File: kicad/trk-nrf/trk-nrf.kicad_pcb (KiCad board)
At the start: 2 copper layers, 35 x 25 mm, 42 parts, among them U1 nRF9151-LAXX, U2 CDCE6214RGER, U3 TPS631010YBGR, U4 TPS631010YBGR, X1 TG2520SMN-xx.xxxxxxMhz-xxxxNM

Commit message: Updates - pre-routing
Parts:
- added J1: Conn_02x05_Odd_Even, Connector_PinHeader_1.00mm:PinHeader_2x05_P1.00mm_Vertical_SMD, B.Cu at (166.6, 91.7)
- C1: footprint Capacitor_SMD:C_1206_3216Metric -> Capacitor_SMD:C_0805_2012Metric
- R11: footprint Resistor_SMD:R_0603_1608Metric -> Resistor_SMD:R_0402_1005Metric
- TP1, TP2: footprint TestPoint:TestPoint_THTPad_D2.5mm_Drill1.2mm -> TestPoint:TestPoint_Pad_1.5x1.5mm
- TP3: value WSPR N -> WSPR_ANT_N
- TP4: value WSPR P -> WSPR _ANT_P
- TP5, TP6: footprint TestPoint:TestPoint_THTPad_D2.5mm_Drill1.2mm -> TestPoint:TestPoint_THTPad_D1.5mm_Drill0.7mm
- U3, U4: footprint footprints:YBG0008-MFG -> footprints:YBG0008
- moved R7 135.4 mm to (172.0, 105.5), turned to 90 degrees
- moved C7 134.2 mm to (170.5, 106.0), turned to 180 degrees
- moved C12 133.8 mm to (170.5, 105.0), turned to 180 degrees
- moved R8 132.2 mm to (172.0, 97.5), turned to -90 degrees
- moved C8 131.5 mm to (172.0, 95.5), turned to 90 degrees
- moved TP3 128.9 mm to (170.5, 108.0)
- moved R9 127.2 mm to (167.0, 96.5), turned to 90 degrees
- moved TP1 125.6 mm to (166.5, 108.6)
- moved R1 124.6 mm to (165.2, 93.8), turned to 90 degrees
- moved R2 123.9 mm to (165.2, 91.8), turned to 90 degrees
- moved R11 123.4 mm to (170.0, 94.0), turned to 90 degrees
- moved TP4 123.0 mm to (170.6, 90.8), turned to 180 degrees
- moved C11 122.5 mm to (162.8, 94.5)
- moved R10 122.0 mm to (155.5, 108.5)
- moved TP2 121.9 mm to (162.4, 108.6)
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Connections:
- net /TCXO_REFCLK renamed Net-(U2A-PRIREF_P)
- net Net-(U1-ENABLE) renamed /+3.3V_Ferrite
- net Net-(U1-~{RESET}) renamed /nRF_nRESET
- net Net-(U3-FB) renamed /FB_1.8
- net Net-(U4-FB) renamed /FB_3.3
- R14 pad 2: unconnected-(R14-Pad2) -> /MON_V3P3
- U1 pad 53: unconnected-(U1-COEX1-Pad53) -> /1PPS
- U1 pad 64: unconnected-(U1-P0.07-Pad64) -> /1PPS
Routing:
- net GND: vias 0 -> 10
- added copper zone on F.Cu, net GND
- added copper zone on In2.Cu, net VBUS
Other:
- board size 35 x 25 mm -> 23.2 x 22 mm
- copper layers 2 -> 4

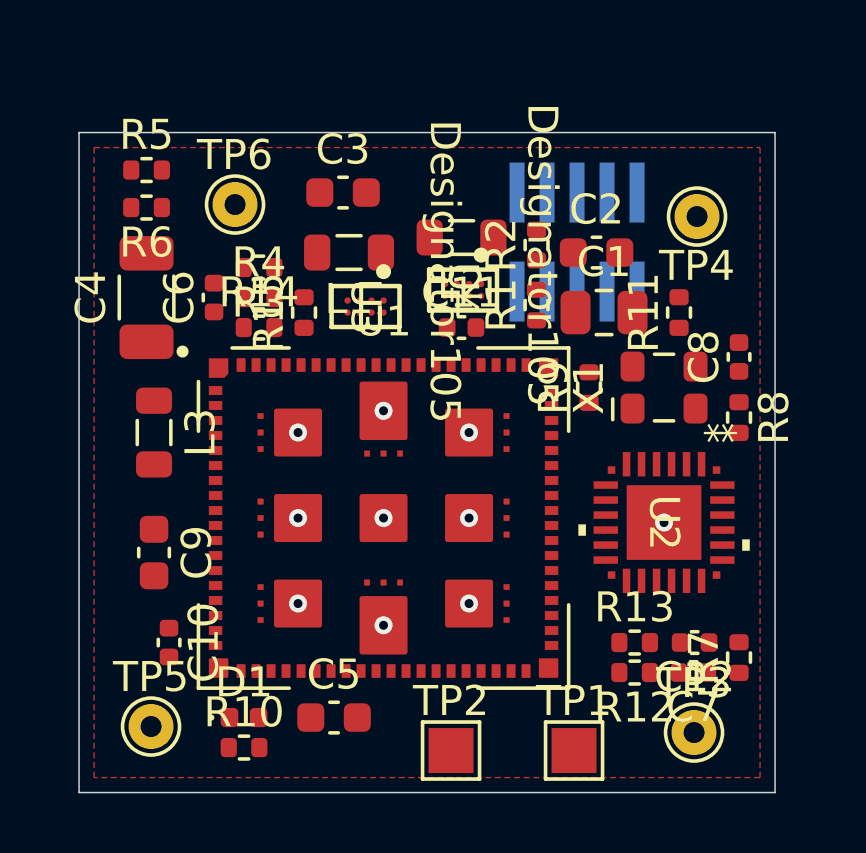
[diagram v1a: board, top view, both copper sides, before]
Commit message: Schematic edits and drc changes
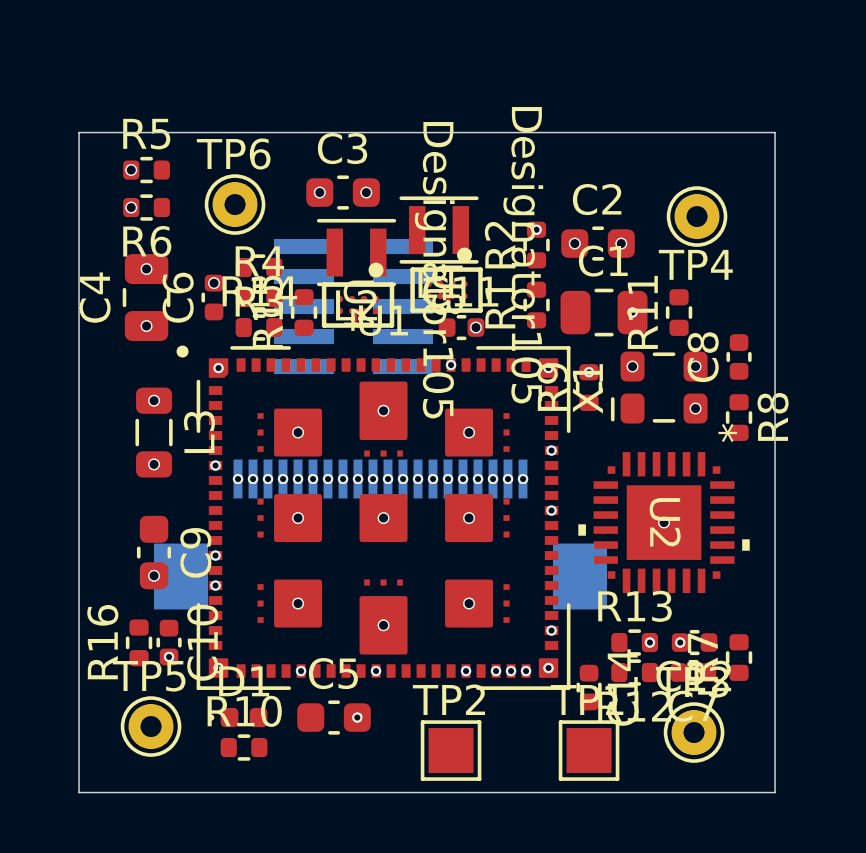
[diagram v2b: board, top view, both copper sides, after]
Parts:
- added C14: 39pF, Capacitor_SMD:C_0402_1005Metric, F.Cu at (167.0, 106.5)
- added J2: Conn_01x20_Pin, Connector_FFC-FPC:Hirose_FH12-20S-0.5SH_1x20-1MP_P0.50mm_Horizontal, B.Cu at (160.1, 101.4)
- added R16: 91K, Resistor_SMD:R_0402_1005Metric, F.Cu at (152.0, 105.0)
- C4: footprint Capacitor_SMD:C_1206_3216Metric -> Capacitor_SMD:C_0805_2012Metric
- C7, C8: value 100nF -> .1uF
- L1, L2: value 2.0uH -> 1.0uH; footprint Inductor_SMD:L_0805_2012Metric -> Inductor_SMD:L_Murata_DFE201610P
- moved J1 7.75 mm to (159.2, 93.8), turned to 0 degrees
- moved L2 3.54 mm to (159.2, 92.0)
- moved U4 3.54 mm to (159.3, 93.8)
- moved L1 3.09 mm to (162.0, 91.2)
- moved U3 2.76 mm to (162.2, 93.2)
- moved TP1 0.50 mm to (167.0, 108.6)
- moved C2 0.30 mm to (167.3, 91.7)
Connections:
- net Net-(U2A-PRIREF_P) renamed /TCXO_REFCLK
- C1 pad 1: +1V8 -> +1.8V
- C11 pad 1: +1V8 -> +1.8V
- J1 pad 7: /nrf_nRESET -> /nRF_nRESET
- J1 pad 9: /+1.8V -> +1.8V
- R1 pad 1: +1V8 -> +1.8V
- R10 pad 1: +1V8 -> +1.8V
- R11 pad 1: +1V8 -> +1.8V
- R12 pad 1: +1V8 -> +1.8V
- TP1 pad 1: Net-(U1-GPS) -> Net-(C14-Pad2)
- U1 pad 10: /+3.3V_Ferrite -> Net-(U1-ENABLE)
- U1 pad 19: +1V8 -> +1.8V
- U1 pad 2: unconnected-(U1-P0.20/AIN7-Pad2) -> /AIN7
- U1 pad 44: unconnected-(U1-P0.26-Pad44) -> /P0.26
- U1 pad 45: unconnected-(U1-P0.27-Pad45) -> /P0.27
- U1 pad 47: unconnected-(U1-P0.28-Pad47) -> /P0.28
- U1 pad 48: unconnected-(U1-P0.29-Pad48) -> /P0.29
- U1 pad 49: unconnected-(U1-P0.30-Pad49) -> /P0.30
- U1 pad 65: +1V8 -> +1.8V
- U1 pad 67: unconnected-(U1-P0.08-Pad67) -> /PO.08
- U1 pad 68: unconnected-(U1-P0.09-Pad68) -> /P0.09
- U1 pad 69: unconnected-(U1-P0.10-Pad69) -> /P0.10
- U1 pad 70: unconnected-(U1-P0.11-Pad70) -> /P0.11
- U1 pad 72: unconnected-(U1-P0.12-Pad72) -> /P0.12
- U1 pad 77: unconnected-(U1-P0.16/AIN3-Pad77) -> /AIN3
- U1 pad 78: unconnected-(U1-P0.17/AIN4-Pad78) -> /AIN4
- U1 pad 79: unconnected-(U1-P0.18/AIN5-Pad79) -> /AIN5
- U1 pad 80: unconnected-(U1-P0.19/AIN6-Pad80) -> /AIN6
- U2 pad 12: /SCLK -> /SCL
- U3 pad D1: +1V8 -> +1.8V
- X1 pad 4: +1V8 -> +1.8V
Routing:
- net GND: track 0.00 -> 1.50 mm, vias 10 -> 44
- net VBUS: vias 0 -> 4
- net /TCXO_REFCLK: vias 0 -> 1
- net /PO.08: vias 0 -> 1
- net /P0.30: vias 0 -> 1
- net /P0.29: vias 0 -> 1
- net /P0.28: vias 0 -> 1
- net /P0.27: vias 0 -> 1
- net /P0.26: vias 0 -> 1
- net /P0.12: vias 0 -> 1
- net /P0.11: vias 0 -> 1
- net /P0.10: vias 0 -> 1
- net /P0.09: vias 0 -> 1
- net /AIN7: vias 0 -> 1
- net /AIN6: vias 0 -> 1
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- added copper zone on In1.Cu, net GND
- removed copper zone on F.Cu, net GND
- removed copper zone on In2.Cu, net VBUS

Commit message: Updated schematic
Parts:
- moved J1 0.81 mm to (159.1, 93.0)
- moved TP6 0.71 mm to (154.5, 90.3)
- turned X1 to -90 degrees
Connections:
- J2 pad 12: /AIN7 -> /MON_VBUS
- U1 pad 2: /AIN7 -> /MON_VBUS
- U1 pad 73: /MON_VBUS -> /AIN0
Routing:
- net GND: vias 44 -> 45
- net /TCXO_REFCLK: vias 1 -> 0
- net /PO.08: vias 1 -> 2
- net /PLL_GPIO4: vias 0 -> 1
- net /P0.11: vias 1 -> 2
- net /P0.10: vias 1 -> 2
- net /P0.09: vias 1 -> 2
- net /MON_VBUS: vias 0 -> 1
- net /MON_V1P8: vias 0 -> 1
- net /AIN7: vias 1 -> 0
- net /AIN6: vias 1 -> 2
- net /AIN5: vias 1 -> 2
- net /AIN4: vias 1 -> 2
- net /AIN3: vias 1 -> 2
- net /1PPS: vias 0 -> 1
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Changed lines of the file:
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@@
 	(net 57 "unconnected-(U1-VIO-Pad29)")
 	(net 58 "/AIN5")
-	(net 59 "/AIN7")
+	(net 59 "/AIN0")
 	(net 60 "unconnected-(U1-COEX2-Pad54)")
 	(net 61 "unconnected-(U2A-OUT2_P-Pad18)")
@@
 	(footprint "TestPoint:TestPoint_THTPad_D1.5mm_Drill0.7mm"
 		(layer "F.Cu")
-		(at 155.2 90.4)
+		(at 154.5 90.3)
 		(descr "THT pad as test Point, diameter 1.5mm, hole diameter 0.7mm")
 		(tags "test point THT pad")
@@
 			(layers "F.Cu" "F.Paste" "F.Mask")
 			(roundrect_rratio 0.05)
-			(net 59 "/AIN7")
+			(net 95 "/MON_VBUS")
 			(pinfunction "P0.20/AIN7")
 			(pintype "bidirectional")
@@
 			(layers "F.Cu" "F.Paste" "F.Mask")
 			(roundrect_rratio 0.05)
-			(net 95 "/MON_VBUS")
+			(net 59 "/AIN0")
 			(pinfunction "P0.13/AIN0")
 			(pintype "bidirectional")
@@
 		(placed yes)
 		(layer "F.Cu")
-		(at 169.5 96.5 90)
+		(at 169.5 96.5 -90)
 		(descr "Miniature Crystal Clock Oscillator TG2520 series, https://support.epson.biz/td/api/doc_check.php?dl=app_TG2520SMN&lang=en")
 		(tags "Miniature Crystal Clock Oscillator TG2520 series SMD SMT")
@@
 		)
 		(property "Footprint" "Oscillator:Oscillator_SMD_SeikoEpson_TG2520SMN-xxx-xxxxxx-4Pin_2.5x2.0mm"
-			(at 0 0 90)
+			(at 0 0 -90)
 			(unlocked yes)
 			(layer "F.Fab")
@@
 		)
 		(property "Datasheet" "https://support.epson.biz/td/api/doc_check.php?dl=app_TG2520SMN&lang=en"
-			(at 0 0 90)
+			(at 0 0 -90)
 			(unlocked yes)
 			(layer "F.Fab")
@@
 		)
 		(property "Description" "Crystal Oscillator Low Profile / High Stability TCXO"
-			(at 0 0 90)
+			(at 0 0 -90)
 			(unlocked yes)
 			(layer "F.Fab")
@@
 		)
 		(property "JLCPCB Part Number" "C3007519"
-			(at 0 0 90)
+			(at 0 0 -90)
 			(unlocked yes)
 			(layer "F.Fab")
@@
 		(attr smd)
 		(fp_line
-			(start -0.38 -1.71)
-			(end -1.07 -1.71)
+			(start -1.11 0.32)
+			(end -1.11 -0.32)
 			(stroke
 				(width 0.12)
@@
 		)
 		(fp_line
-			(start -1.11 0.32)
-			(end -1.11 -0.32)
+			(start -0.38 -1.71)
+			(end -1.07 -1.71)
 			(stroke
 				(width 0.12)
@@
 		)
 		(fp_line
-			(start 1.45 -1.7)
+			(start -1.45 1.7)
 			(end 1.45 1.7)
 			(stroke
@@
 		(fp_line
 			(start -1.45 -1.7)
-			(end 1.45 -1.7)
+			(end -1.45 1.7)
 			(stroke
 				(width 0.05)
@@
 		(fp_line
 			(start -1.45 -1.7)
-			(end -1.45 1.7)
+			(end 1.45 -1.7)
 			(stroke
 				(width 0.05)
@@
 		)
 		(fp_line
-			(start -1.45 1.7)
+			(start 1.45 -1.7)
 			(end 1.45 1.7)
 			(stroke
@@
 		)
 		(fp_line
-			(start 1 -1.25)
+			(start -1 1.25)
 			(end 1 1.25)
 			(stroke
@@
 		)
 		(fp_line
-			(start -0.5 -1.25)
-			(end 1 -1.25)
+			(start -1 -0.75)
+			(end -1 1.25)
 			(stroke
 				(width 0.1)
@@
 		)
 		(fp_line
-			(start -1 -0.75)
-			(end -1 1.25)
+			(start -0.5 -1.25)
+			(end 1 -1.25)
 			(stroke
 				(width 0.1)
@@
 		)
 		(fp_line
-			(start -1 1.25)
+			(start 1 -1.25)
 			(end 1 1.25)
 			(stroke
@@
 		)
 		(fp_text user "${REFERENCE}"
-			(at 0 0 0)
+			(at 0 0 360)
 			(layer "F.Fab")
 			(effects
@@
 		)
 		(pad "1" smd roundrect
-			(at -0.7 -1.05 90)
+			(at -0.7 -1.05 270)
 			(size 1 0.8)
 			(layers "F.Cu" "F.Paste" "F.Mask")
@@
 		)
 		(pad "2" smd roundrect
-			(at -0.7 1.05 90)
+			(at -0.7 1.05 270)
 			(size 1 0.8)
 			(layers "F.Cu" "F.Paste" "F.Mask")
@@
 		)
 		(pad "3" smd roundrect
-			(at 0.7 1.05 90)
+			(at 0.7 1.05 270)
 			(size 1 0.8)
 			(layers "F.Cu" "F.Paste" "F.Mask")
@@
 		)
 		(pad "4" smd roundrect
-			(at 0.7 -1.05 90)
+			(at 0.7 -1.05 270)
 			(size 1 0.8)
 			(layers "F.Cu" "F.Paste" "F.Mask")
@@
 			(polygon
 				(pts
-					(xy 168.2 96.65) (xy 168.2 96.35) (xy 168.9 96.35) (xy 168.9 95.5) (xy 170.1 95.5) (xy 170.1 96.35)
-					(xy 170.75 96.35) (xy 170.75 96.65) (xy 170.1 96.65) (xy 170.1 97.5) (xy 168.9 97.5) (xy 168.9 96.65)
+					(xy 170.8 96.35) (xy 170.8 96.65) (xy 170.1 96.65) (xy 170.1 97.5) (xy 168.9 97.5) (xy 168.9 96.65)
+					(xy 168.25 96.65) (xy 168.25 96.35) (xy 168.9 96.35) (xy 168.9 95.5) (xy 170.1 95.5) (xy 170.1 96.35)
 				)
 			)
@@
 	(footprint "Connector_PinHeader_1.00mm:PinHeader_2x05_P1.00mm_Vertical_SMD"
 		(layer "B.Cu")
-		(at 159.15 93.8)
+		(at 159.05 93)
 		(descr "surface-mounted straight pin header, 2x05, 1.00mm pitch, double rows")
 		(tags "Surface mounted pin header SMD 2x05 1.00mm double row")
@@
 			(size 0.3 1.3)
 			(layers "B.Cu" "B.Paste" "B.Mask")
-			(net 59 "/AIN7")
+			(net 95 "/MON_VBUS")
 			(pinfunction "Pin_12")
 			(pintype "passive")
@@
 	)
 	(via
+		(at 156.9 95.75)
+		(size 0.35)
+		(drill 0.2)
+		(layers "F.Cu" "B.Cu")
+		(net 21)
+	)
+	(via
 		(at 161.3 99.55)
 		(size 0.35)
@@
 	)
 	(via
+		(at 163.4 95.75)
+		(size 0.35)
+		(drill 0.2)
+		(layers "F.Cu" "B.Cu")
+		(net 23)
+	)
+	(via
 		(at 157.3 99.55)
 		(size 0.35)
@@
 	)
 	(via
+		(at 161.9 95.75)
+		(size 0.35)
+		(drill 0.2)
+		(layers "F.Cu" "B.Cu")
+		(net 25)
+	)
+	(via
 		(at 163.8 99.55)
 		(size 0.35)
@@
 	)
 	(via
+		(at 160.4 95.75)
+		(size 0.35)
+		(drill 0.2)
+		(layers "F.Cu" "B.Cu")
+		(net 37)
+	)
+	(via
 		(at 162.3 99.55)
 		(size 0.35)
@@
 	)
 	(via
+		(at 160.9 95.75)
+		(size 0.35)
+		(drill 0.2)
+		(layers "F.Cu" "B.Cu")
+		(net 47)
+	)
+	(via
 		(at 163.3 99.55)
 		(size 0.35)
@@
 	)
 	(via
+		(at 161.4 95.75)
+		(size 0.35)
+		(drill 0.2)
+		(layers "F.Cu" "B.Cu")
+		(net 49)
+	)
+	(via
+		(at 155.4 95.75)
+		(size 0.35)
+		(drill 0.2)
+		(layers "F.Cu" "B.Cu")
+		(net 52)
+	)
+	(via
 		(at 159.8 99.55)
 		(size 0.35)
@@
 	)
 	(via
-		(at 159.3 99.55)
+		(at 155.9 95.75)
 		(size 0.35)
 		(drill 0.2)
 		(layers "F.Cu" "B.Cu")
-		(net 59)
+		(net 58)
 	)
 	(segment
@@
 	)
 	(via
-		(at 170.55 97.2)
-		(size 0.4)
-		(drill 0.3)
-		(layers "F.Cu" "B.Cu")
-		(net 69)
-	)
-	(via
 		(at 152.25 92.55)
 		(size 0.4)
@@
 	)
 	(via
+		(at 168.45 95.8)
+		(size 0.35)
+		(drill 0.2)
+		(layers "F.Cu" "B.Cu")
+		(net 69)
+	)
+	(via
 		(at 165.75 100.6)
 		(size 0.35)
@@
 	)
 	(via
+		(at 157.4 95.75)
+		(size 0.35)
+		(drill 0.2)
+		(layers "F.Cu" "B.Cu")
+		(net 69)
+	)
+	(via
 		(at 169.03 105)
 		(size 0.35)
@@
 	)
 	(via
+		(at 159.3 99.55)
+		(size 0.35)
+		(drill 0.2)
+		(layers "F.Cu" "B.Cu")
+		(net 95)
+	)
+	(via
+		(at 158.4 95.75)
+		(size 0.35)
+		(drill 0.2)
+		(layers "F.Cu" "B.Cu")
+		(net 96)
+	)
+	(via
+		(at 163.9 95.75)
+		(size 0.35)
+		(drill 0.2)
+		(layers "F.Cu" "B.Cu")
+		(net 101)
+	)
+	(via
+		(at 156.4 95.75)
+		(size 0.35)
+		(drill 0.2)
+		(layers "F.Cu" "B.Cu")
+		(net 107)
+	)
+	(via
 		(at 160.8 99.55)
 		(size 0.35)
@@
 	)
 	(via
-		(at 168.45 95.8)
-		(size 0.4)
-		(drill 0.3)
+		(at 170.55 97.2)
+		(size 0.35)
+		(drill 0.2)
 		(layers "F.Cu" "B.Cu")
 		(net 108)
 	)
 	(via
-		(at 155.8 99.55)
+		(at 170 94.51)
 		(size 0.35)
 		(drill 0.2)
@@
 	)
 	(via
-		(at 170.55 95.8)
-		(size 0.4)
-		(drill 0.3)
+		(at 155.8 99.55)
+		(size 0.35)
+		(drill 0.2)
 		(layers "F.Cu" "B.Cu")
-		(net 109)
+		(net 108)
 	)
 	(zone

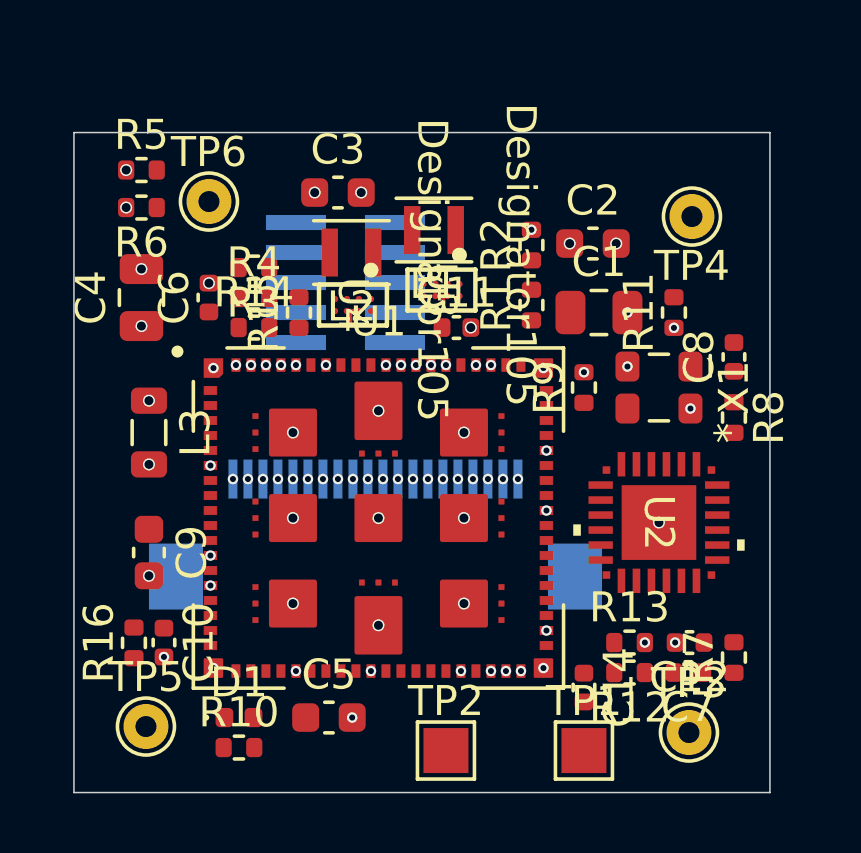
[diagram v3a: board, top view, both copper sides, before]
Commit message: Add second ground and freeroute board
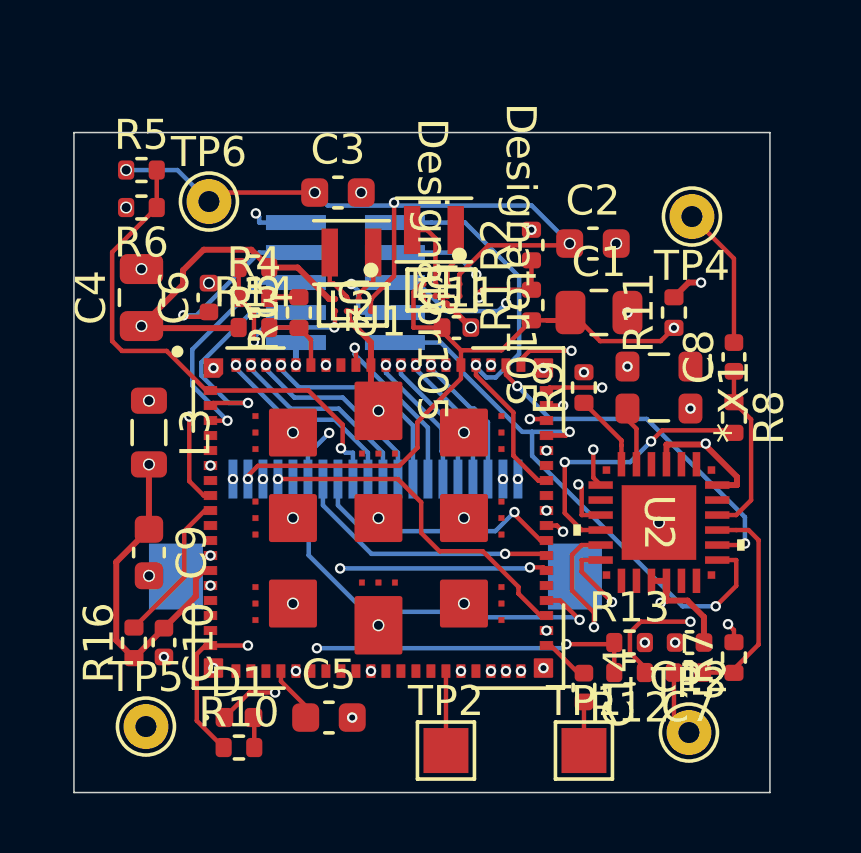
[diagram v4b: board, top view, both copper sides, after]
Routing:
- net +1.8V: track 0.00 -> 60.2 mm, vias 3 -> 6
- net VBUS: track 0.00 -> 35.3 mm, vias 4 -> 5
- net Net-(U2B-VDDO_12): track 0.00 -> 23.1 mm, vias 0 -> 3
- net /SCL: track 0.00 -> 21.5 mm, vias 0 -> 3
- net /MON_V1P8: track 0.00 -> 20.5 mm, vias 1 -> 3
- net /SDA: track 0.00 -> 19.5 mm, vias 0 -> 2
- net +3.3V: track 0.00 -> 18.4 mm
- net /PLL_GPIO4: track 0.00 -> 17.5 mm, vias 1 -> 2
- net /MON_VBUS: track 0.00 -> 17.3 mm
- net /DEBUG_LED: track 0.00 -> 14.5 mm, vias 0 -> 2
- net /1PPS: track 0.00 -> 14.4 mm
- net /P0.27: track 0.00 -> 14.1 mm
- net /P0.28: track 0.00 -> 13.5 mm, vias 1 -> 3
- net Net-(U2A-OUT4_N): track 0.00 -> 12.3 mm, vias 0 -> 2
- net /PLL_GPIO1: track 0.00 -> 12.1 mm, vias 0 -> 2
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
